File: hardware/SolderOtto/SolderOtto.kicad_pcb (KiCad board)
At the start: 4 copper layers, 120 x 60 mm, 226 parts, among them J201 Conn_02x04_Counter_Clockwise, J301 TC-2050, J401 Conn_01x20, J501 Conn_01x08, J601 Conn_01x07, P301 USB_C_Plug_USB2.0, Q201 T2N7002AK, Q202 BC858B, Q203 BC847A, Q204 BC847A, Q801 Q_Dual_NMOS, Q802 Q_Dual_NMOS, Q803 Q_Dual_NMOS, Q804 DTD123EK, Q805 DTD123EK, Q806 DTD123EK, Q807 Q_Dual_NMOS, Q808 Q_Dual_NMOS, Q809 DTD123EK, Q810 DTD123EK, Q901 BC847A, Q902 BC858B, Q903 BC847A, SW301 SW_Push, U201 LM5012, U202 AP3211K, U203 AP3211K, U204 AP3211K, U205 LM27761, U206 MCP9701T-E/TT, U301 USBLC6-2SC6, U302 STM32G474QETx, U303 MX25R3235FM1xx0, U701 SN74LVC125A, U702 TS5A3159ADCK, U801 VOM1271, U802 VOM1271, U803 VOM1271, U804 VOM1271, U805 VOM1271, U901 OPA202, U902 LM358B, U903 74hc4053, U904 OPA202, U905 OPA202, Y301 32.768 kHz

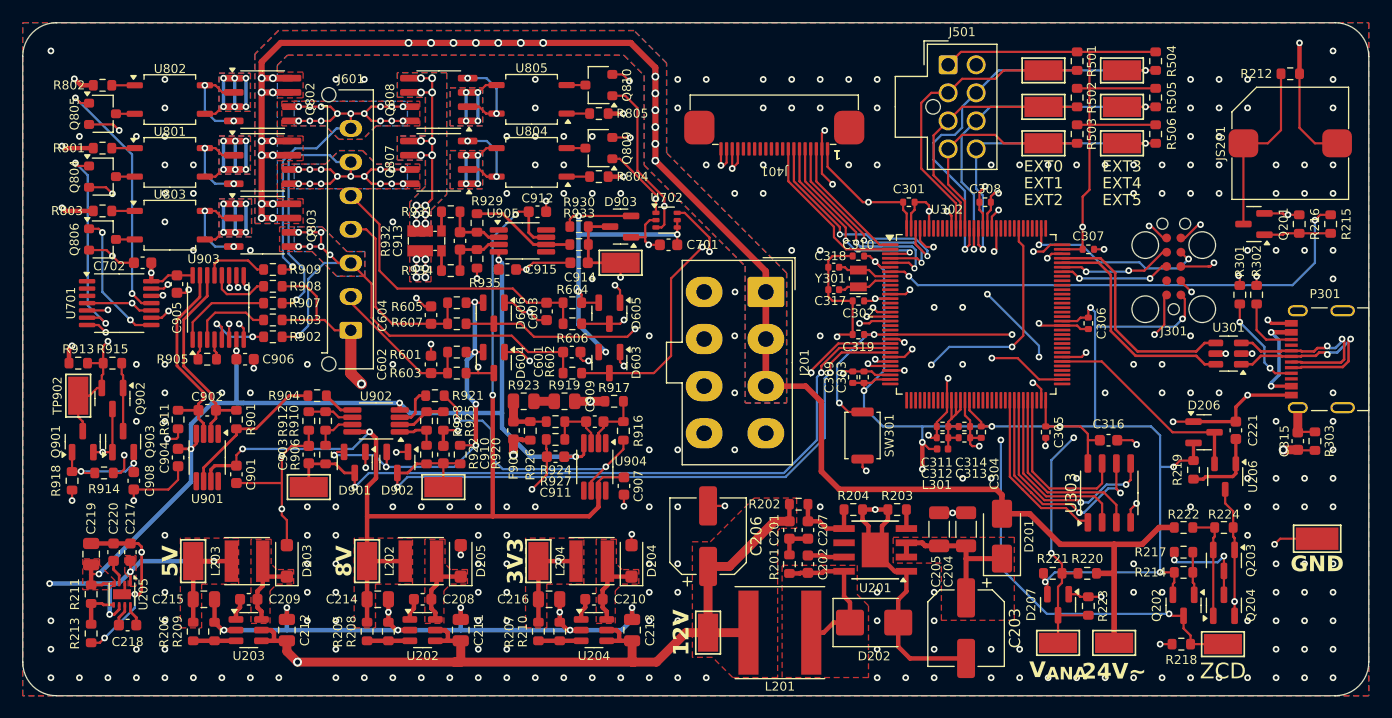
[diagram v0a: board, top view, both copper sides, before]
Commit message: add via stichting
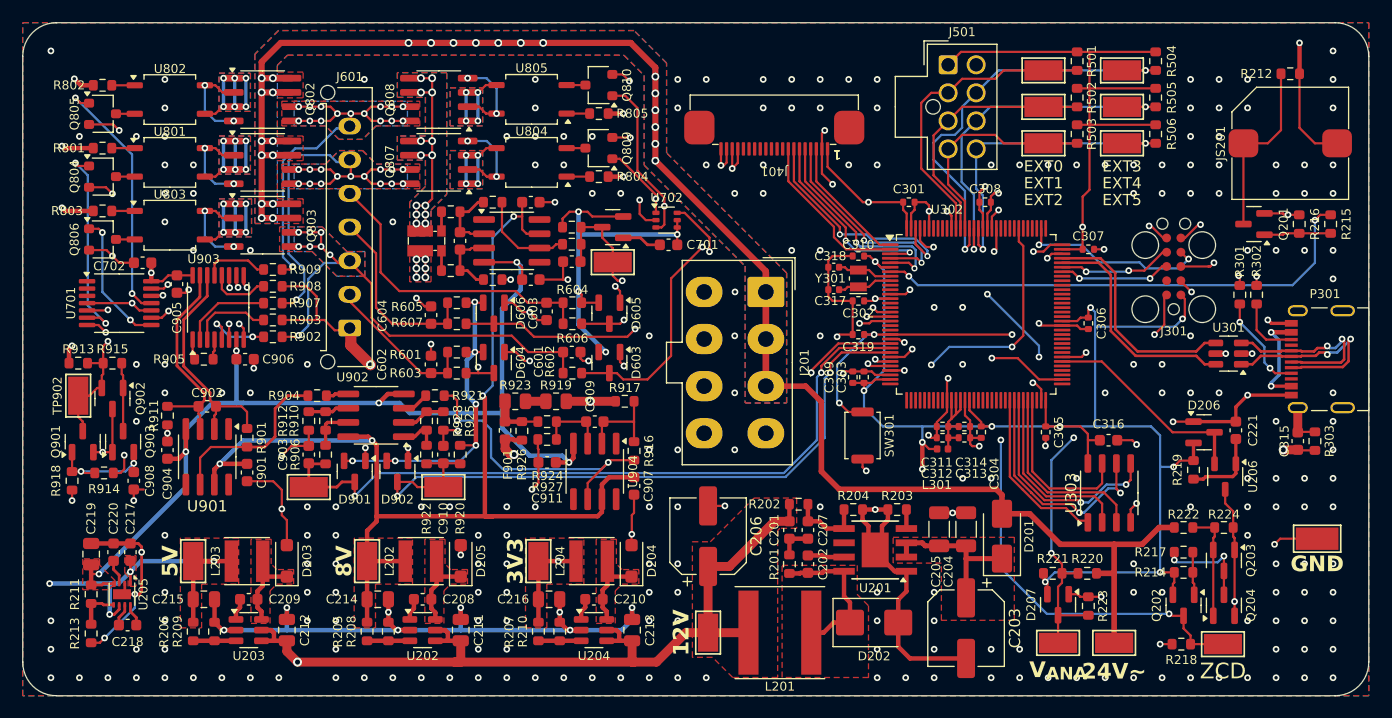
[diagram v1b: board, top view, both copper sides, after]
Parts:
- U901, U902, U904, U905: footprint Package_SO:VSSOP-8_3x3mm_P0.65mm -> Package_SO:SOIC-8_3.9x4.9mm_P1.27mm
- moved R935 2.32 mm to (151.9, 72.9), turned to 180 degrees
- moved R929 2.32 mm to (151.9, 66.0), turned to 0 degrees
- moved C915 2.27 mm to (155.3, 72.9)
- moved R916 2.02 mm to (164.5, 88.2)
- moved R901 1.88 mm to (130.0, 87.0)
- moved C904 1.16 mm to (122.9, 88.1), turned to 90 degrees
- moved C912 1.03 mm to (155.3, 66.0)
- moved R911 1.01 mm to (122.9, 85.0)
- moved C901 0.96 mm to (130.0, 90.1)
- moved R917 0.95 mm to (163.7, 83.8)
- moved U905 0.95 mm to (153.6, 69.5)
- moved C911 0.91 mm to (156.8, 89.2)
- moved C907 0.90 mm to (164.5, 91.3)
- moved D901 0.80 mm to (139.6, 90.0)
- moved D902 0.80 mm to (143.4, 90.0)
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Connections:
- R905 pad 2: Net-(U903-2Y0) -> Net-(U903-2Y1)
- R907 pad 2: Net-(U903-2Y1) -> Net-(U903-2Y0)
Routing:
- net Net-(U903-2Y1): track 8.58 -> 1.82 mm
- net -5V: track 87.7 -> 94.3 mm
- net Net-(U903-2Y0): track 1.82 -> 7.97 mm
- net GND: track 824.0 -> 820.8 mm, vias 318 -> 309
- net +8V: track 97.9 -> 100.7 mm
- net Net-(U904A--): track 5.70 -> 8.19 mm
- net +3V3: track 439.8 -> 437.4 mm
- net Net-(R901-Pad2): track 13.5 -> 15.8 mm
- net /Channel0/channel_meas/IN-: track 18.2 -> 20.3 mm
- net /Channel0/I_{LEAK}: track 61.7 -> 63.5 mm
- net /Channel0/T_{TIP}: track 64.3 -> 66.0 mm
- net /Channel0/TC: track 69.7 -> 71.2 mm
- net Net-(R916-Pad2): track 25.0 -> 26.5 mm
- net /Channel0/DET: track 112.1 -> 113.6 mm
- net Net-(U902A-+): track 3.81 -> 2.41 mm
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
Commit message: aisler order
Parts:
- added REF**: MountingHole_2.7mm_M2.5, MountingHole:MountingHole_2.7mm_M2.5, F.Cu at (113.0, 53.0)
- added REF**: MountingHole_2.7mm_M2.5, MountingHole:MountingHole_2.7mm_M2.5, F.Cu at (227.0, 53.0)
- added REF**: MountingHole_2.7mm_M2.5, MountingHole:MountingHole_2.7mm_M2.5, F.Cu at (113.0, 107.0)
- added REF**: MountingHole_2.7mm_M2.5, MountingHole:MountingHole_2.7mm_M2.5, F.Cu at (227.0, 107.0)
- moved JS201 3.25 mm to (219.8, 60.8)
- moved R212 3.25 mm to (219.8, 54.5)
- moved C217 1.26 mm to (120.0, 96.0)
- moved C218 1.26 mm to (119.8, 102.5)
- moved C219 1.26 mm to (116.5, 96.2)
- moved C220 1.26 mm to (118.5, 96.0)
- moved R211 1.26 mm to (116.5, 99.8)
- moved R213 1.26 mm to (116.5, 103.2)
- moved U205 1.26 mm to (119.2, 99.8)
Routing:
- net +5V: track 214.8 -> 206.9 mm
- net Net-(JS201--): track 16.1 -> 18.3 mm
- net GND: track 820.8 -> 818.9 mm, vias 309 -> 313
- net /Channel0/channel_power/COM_SW_HIGH: track 23.0 -> 21.4 mm
- net +12V: track 217.8 -> 216.9 mm

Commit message: change some material numbers
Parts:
- removed REF** (x4): MountingHole_2.7mm_M2.5, MountingHole:MountingHole_2.7mm_M2.5
- D603: value BAS70S -> BAT54SFILM

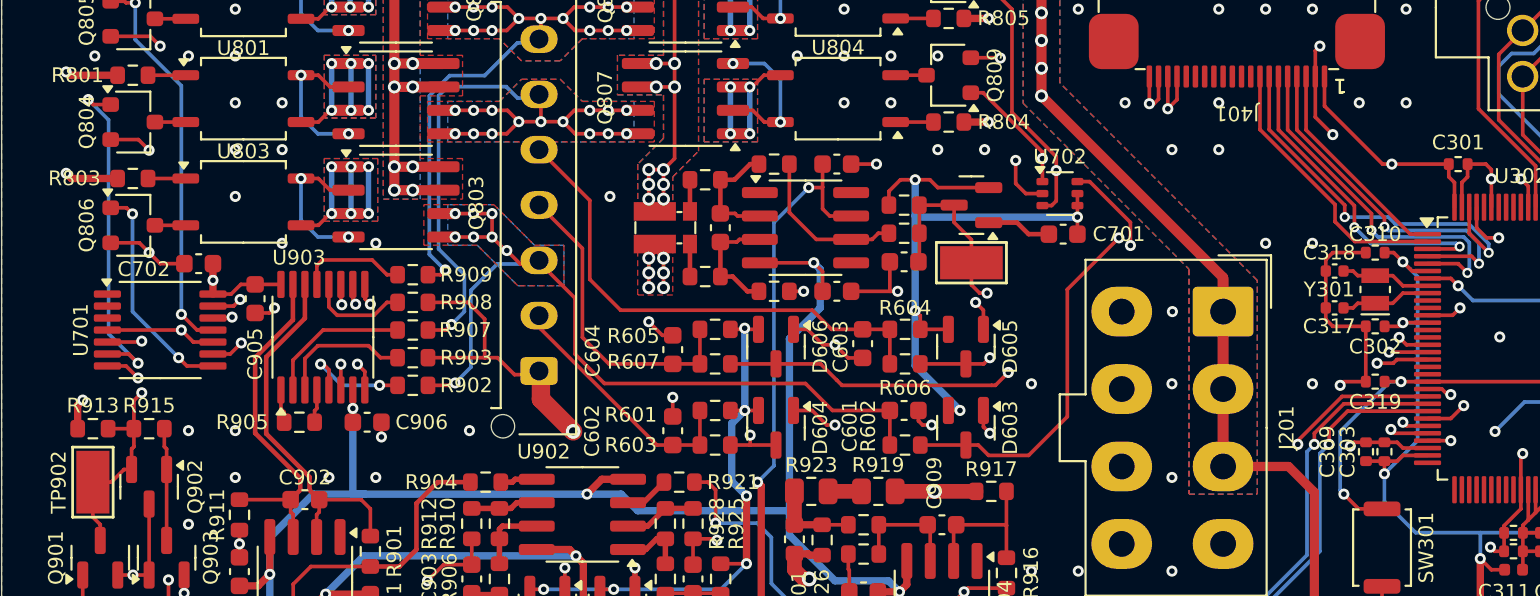
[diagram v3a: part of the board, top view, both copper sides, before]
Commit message: remove low side switching ic
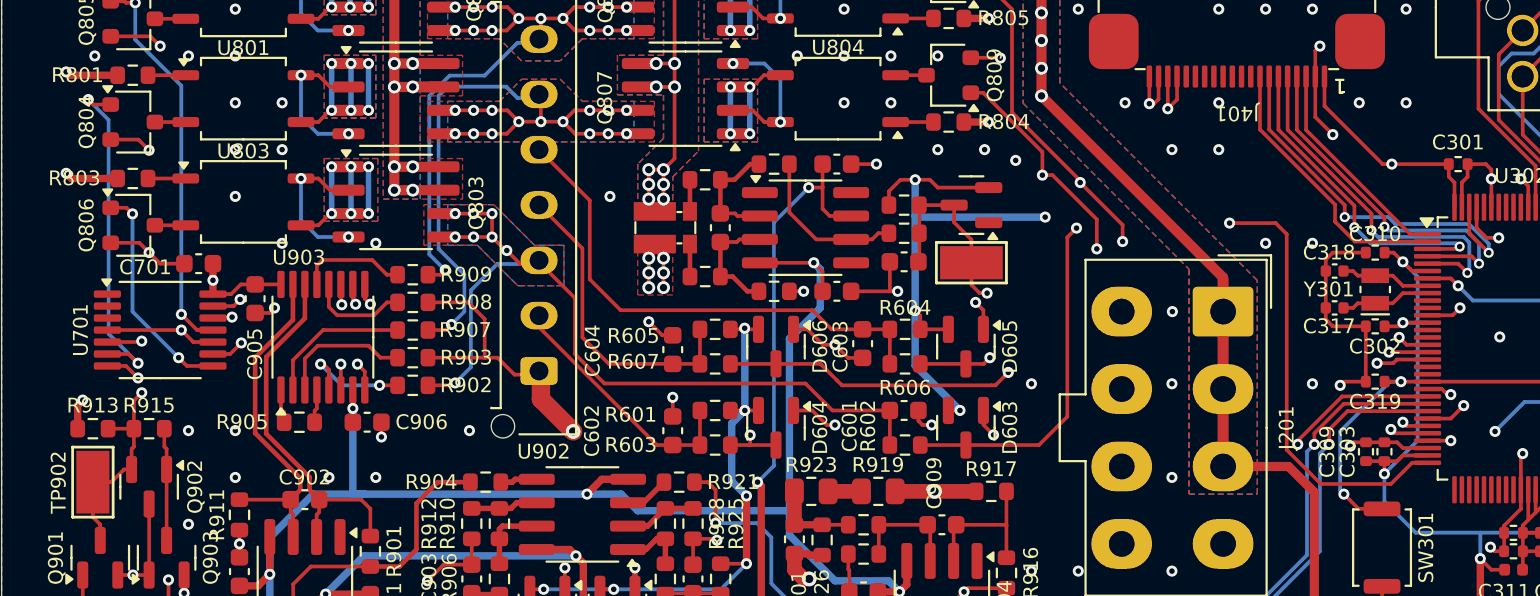
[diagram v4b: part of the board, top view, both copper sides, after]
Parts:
- removed C702: 100n, Capacitor_SMD:C_0603_1608Metric
- removed U702: TS5A3159ADCK, Package_TO_SOT_SMD:SOT-363_SC-70-6
- U206: value MCP9701T-E/TT -> MCP9701T-E/TT
- moved C701 46.9 mm to (120.7, 71.4)
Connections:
- Q809 pad 1: /Channel0/channel_power/LOAD_SW_LOW -> /Channel0/LOW_SIDE_LOAD
- Q810 pad 1: /Channel0/channel_power/COM_SW_LOW -> /Channel0/LOW_SIDE_COM
- U302 pad 26: /Channel0/LOW_SIDE_SW -> /Channel0/LOW_SIDE_LOAD
- U302 pad 32: unconnected-(U302-PA3-Pad32) -> /Channel0/LOW_SIDE_COM
- U701 pad 10: /Channel0/channel_power/LOAD_SW_LOW -> /Channel0/LOW_SIDE_LOAD
- U701 pad 13: /Channel0/channel_power/COM_SW_LOW -> /Channel0/LOW_SIDE_COM
- U701 pad 4: /Channel0/channel_power/LOAD_SW_LOW -> /Channel0/LOW_SIDE_LOAD
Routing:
- net /Channel0/LOW_SIDE_COM: track 0.00 -> 99.0 mm, vias 0 -> 4
- net /Channel0/LOW_SIDE_LOAD: track 0.00 -> 96.1 mm, vias 0 -> 4
- net /Channel0/channel_power/LOAD_SW_LOW: track 63.8 -> 0.00 mm, vias 2 -> 0
- net /Channel0/channel_power/COM_SW_LOW: track 63.7 -> 0.00 mm, vias 2 -> 0
- net /Channel0/LOW_SIDE_SW: track 30.8 -> 0.00 mm, vias 2 -> 0
- net GND: track 818.9 -> 812.6 mm
- net +3V3: track 437.4 -> 435.2 mm
- net /Channel0/iron_sense: track 49.6 -> 50.8 mm

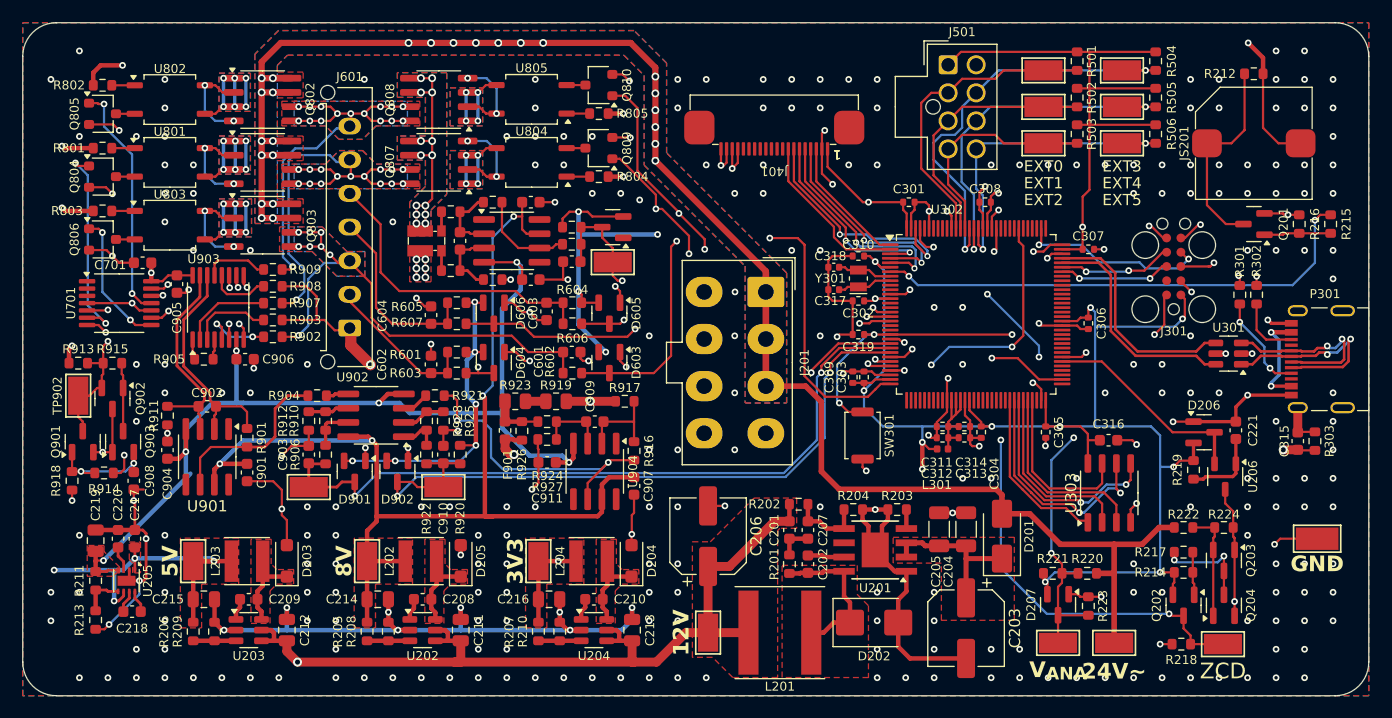
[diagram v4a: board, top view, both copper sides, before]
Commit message: rework pcb due to not working one
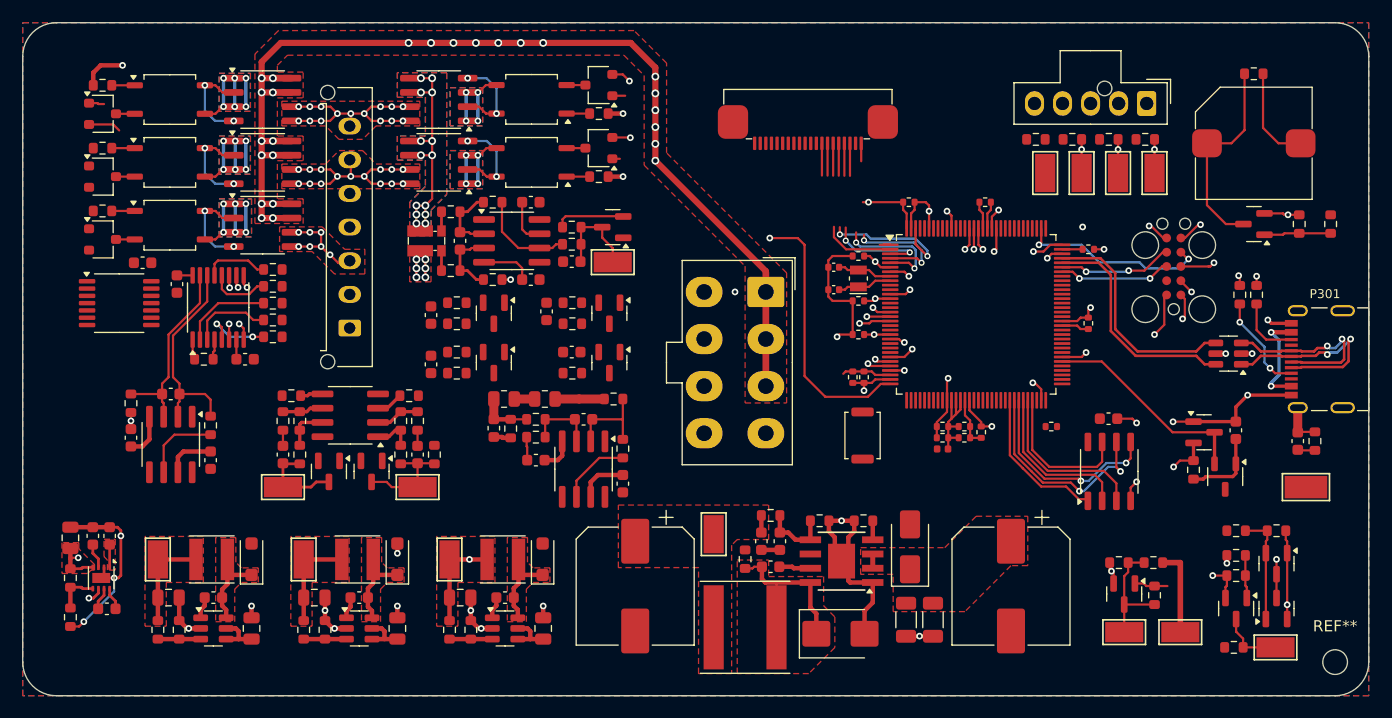
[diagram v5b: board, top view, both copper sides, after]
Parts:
- removed the C908 at (119.9, 90.8)
- removed Q901, Q903: BC847A, Package_TO_SOT_SMD:SOT-23
- removed Q902: BC858B, Package_TO_SOT_SMD:SOT-23
- removed the R501 at (204.0, 53.4)
- removed the R502 at (204.0, 56.7)
- removed the R913 at (115.0, 80.3)
- removed the R914 at (117.2, 90.1)
- removed the R915 at (118.0, 80.3)
- removed the R918 at (114.4, 90.8)
- removed the TP501 at (201.0, 54.2)
- removed the TP502 at (201.0, 57.5)
- removed the TP902 at (115.0, 83.2)
- added REF**: MountingHole_2.2mm_M2, MountingHole:MountingHole_2.2mm_M2, F.Cu at (227.0, 107.0)
- C203, C206: footprint Capacitor_SMD:CP_Elec_6.3x5.7 -> Capacitor_SMD:CP_Elec_10x10
- J501: value Conn_01x08 -> Conn_01x05; footprint Connector_Molex:Molex_Nano-Fit_105310-xx08_2x04_P2.50mm_Vertical -> Connector_Molex:Molex_Nano-Fit_105309-xx05_1x05_P2.50mm_Vertical
- moved J501 18.0 mm to (210.2, 57.2), turned to -90 degrees
- moved R503 10.2 mm to (203.6, 60.4), turned to 0 degrees
- moved TP502 9.83 mm to (204.4, 63.4), turned to -90 degrees
- moved C204 9.68 mm to (188.8, 103.2), turned to -90 degrees
- moved TP202 8.79 mm to (171.6, 95.6)
- moved D201 8.25 mm to (189.1, 96.7)
- moved C205 8.08 mm to (191.2, 103.2), turned to -90 degrees
- moved C210 7.93 mm to (153.0, 101.2)
- moved C216 7.93 mm to (149.0, 101.2)
- moved D204 7.93 mm to (156.3, 97.8)
- moved R210 7.93 mm to (149.9, 104.1)
- moved U204 7.93 mm to (153.0, 104.0)
- moved C213 7.93 mm to (156.4, 104.0)
- moved L204 7.93 mm to (152.8, 97.8)
- moved R207 7.93 mm to (148.1, 104.1)
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- renumbered C909 to C908, C910 to C909, C911 to C910, C912 to C911, C913 to C912, C914 to C913, C915 to C914, R506 to R501, R505 to R502, R504 to R503, R503 to R504, R907 to R905, R905 to R907, R916 to R913, R917 to R914, R919 to R915, R920 to R916, R921 to R917, R922 to R918, R923 to R919, R924 to R920, R925 to R921, R926 to R922, R927 to R923, R928 to R924, R929 to R925, R930 to R926, R931 to R927, R932 to R928, R933 to R929, R934 to R930, R935 to R931, TP503 to TP501, TP504 to TP502, TP505 to TP503, TP506 to TP504, TP903 to TP902, TP904 to TP903
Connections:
- J501 pad 1: +3V3 -> /External connection/EXT_0
- J501 pad 2: /External connection/EXT_5 -> /External connection/EXT_1
- J501 pad 3: /External connection/EXT_4 -> GND
- J501 pad 4: /External connection/EXT_3 -> /External connection/EXT_2
- J501 pad 5: GND -> /External connection/EXT_3
- TP501 pad 1: /External connection/EXT_3 -> /External connection/EXT_0
- TP502 pad 1: /External connection/EXT_2 -> /External connection/EXT_1
- TP503 pad 1: /External connection/EXT_1 -> /External connection/EXT_2
- TP504 pad 1: /External connection/EXT_0 -> /External connection/EXT_3
- U302 pad 116: /External connection/EXT_4 -> /mcu/EXT_4
- U302 pad 117: /External connection/EXT_5 -> /mcu/EXT_5
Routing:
- net GND: track 812.6 -> 157.4 mm, vias 313 -> 44
- net +3V3: track 435.2 -> 56.1 mm, vias 28 -> 12
- net +12V: track 216.9 -> 20.7 mm, vias 6 -> 3
- net +5V: track 206.9 -> 21.1 mm, vias 6 -> 1
- net /Channel0/DET: track 113.6 -> 1.89 mm, vias 2 -> 1
- net /Channel0/LOW_SIDE_LOAD: track 96.1 -> 2.92 mm, vias 4 -> 1
- net +8V: track 100.7 -> 21.9 mm, vias 4 -> 0
- net -5V: track 94.3 -> 17.9 mm, vias 6 -> 1
- net /Channel0/LOW_SIDE_COM: track 99.0 -> 25.1 mm, vias 4 -> 1
- net /Channel0/LOAD0_SW: track 75.8 -> 2.07 mm, vias 2 -> 1
- net Earth: track 76.6 -> 3.01 mm, vias 2 -> 0
- net /Channel0/LOAD1_SW: track 72.4 -> 1.26 mm, vias 2 -> 1
- net /Channel0/COM_SW: track 70.1 -> 1.42 mm, vias 2 -> 1
- net /Channel0/TC: track 71.2 -> 4.39 mm, vias 3 -> 0
- net /Channel0/tip_change: track 63.4 -> 0.00 mm, vias 3 -> 0
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- removed copper zone on B.Cu, net /Channel0/COM
- removed copper zone on B.Cu, net /Channel0/LOAD
- removed copper zone on B.Cu, net /Channel0/_iron_sense
- removed copper zone on B.Cu, net 24V_{AC}
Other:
- board text removed: "1"
